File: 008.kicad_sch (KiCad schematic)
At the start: 38 parts, among them U1 AM6232ASCGHAALWR, U2 4Gbit

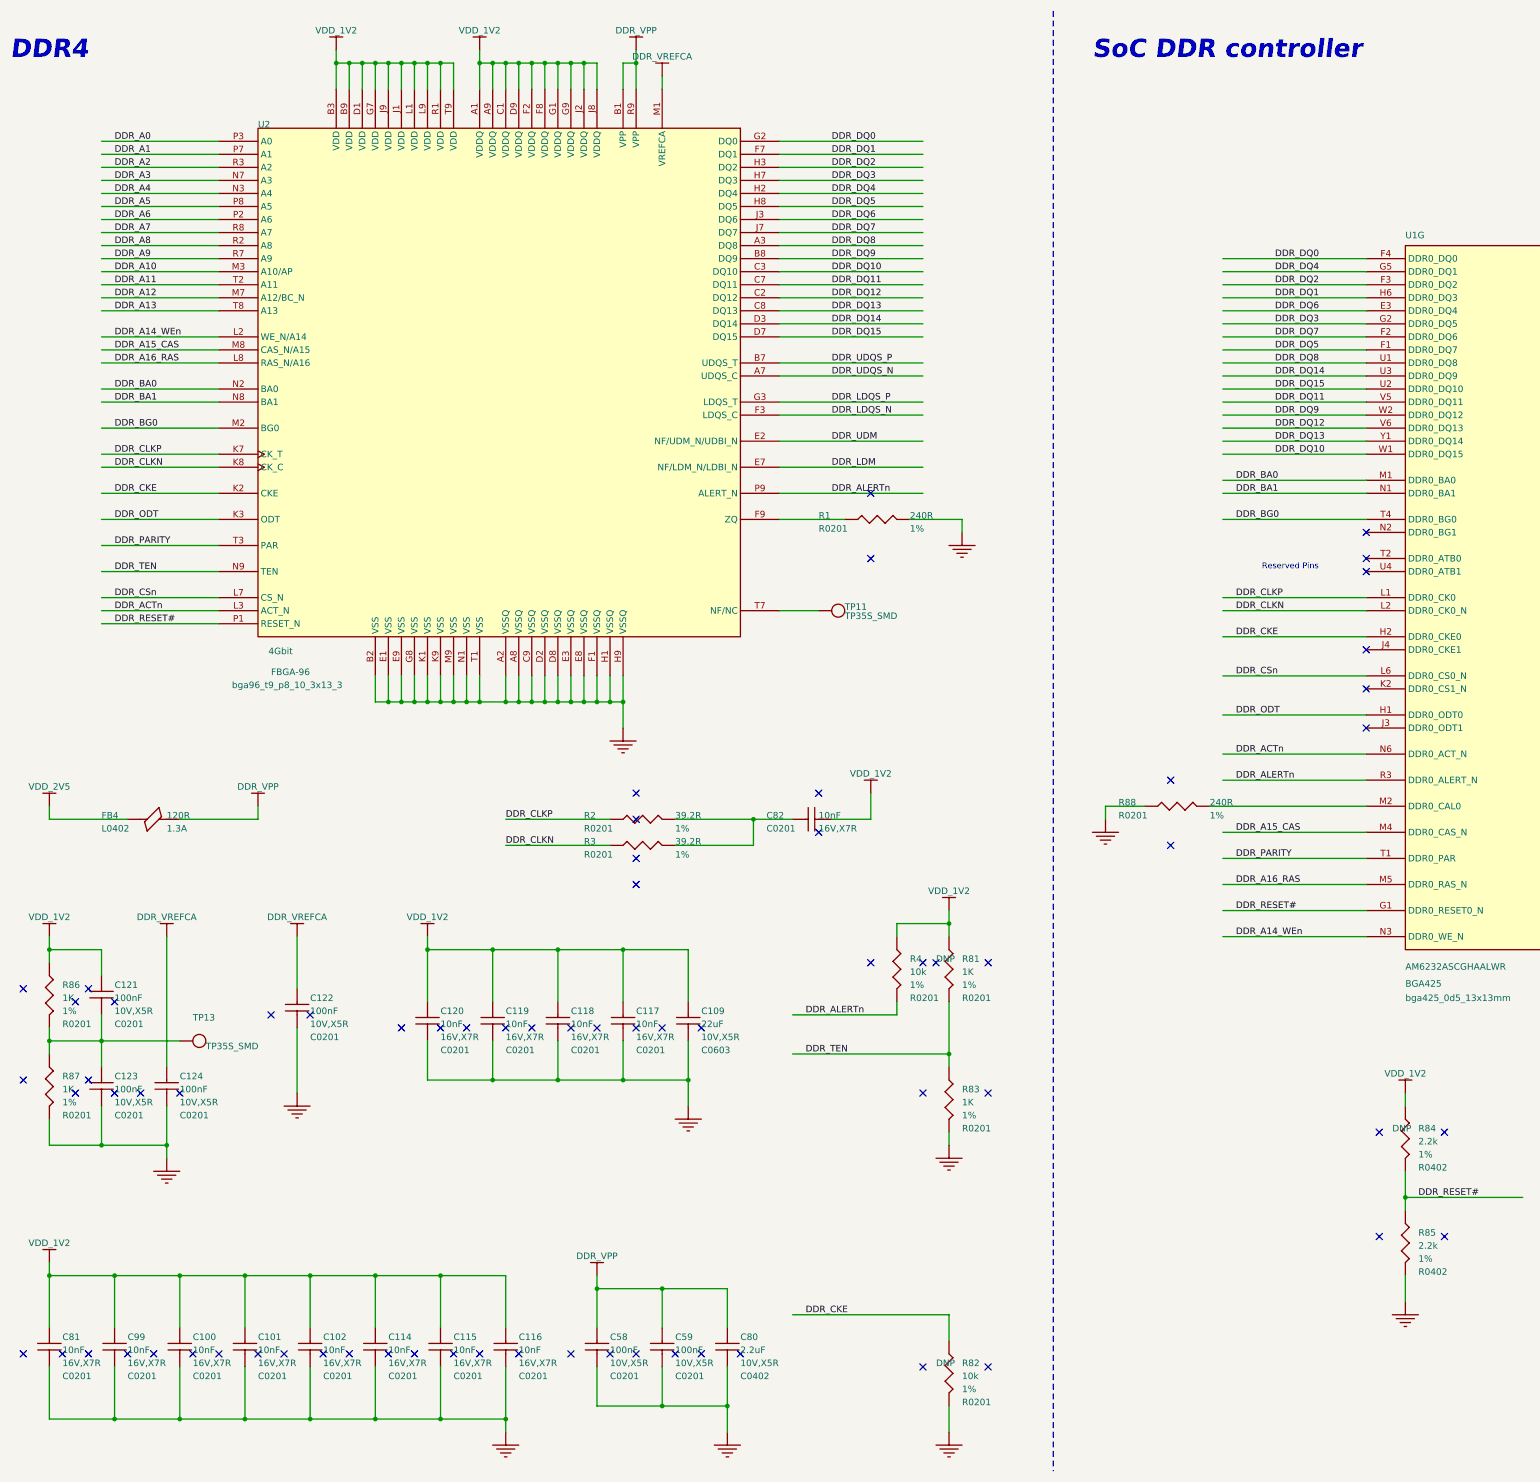
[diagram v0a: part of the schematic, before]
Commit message: Remove rando NCs added during conversion
Also a little tidying.

TODO: check junctions that may be missing. Noticed a few obvious ones
and corrected them already.

Signed-off-by: Michael Welling <mwelling79@gmail.com>
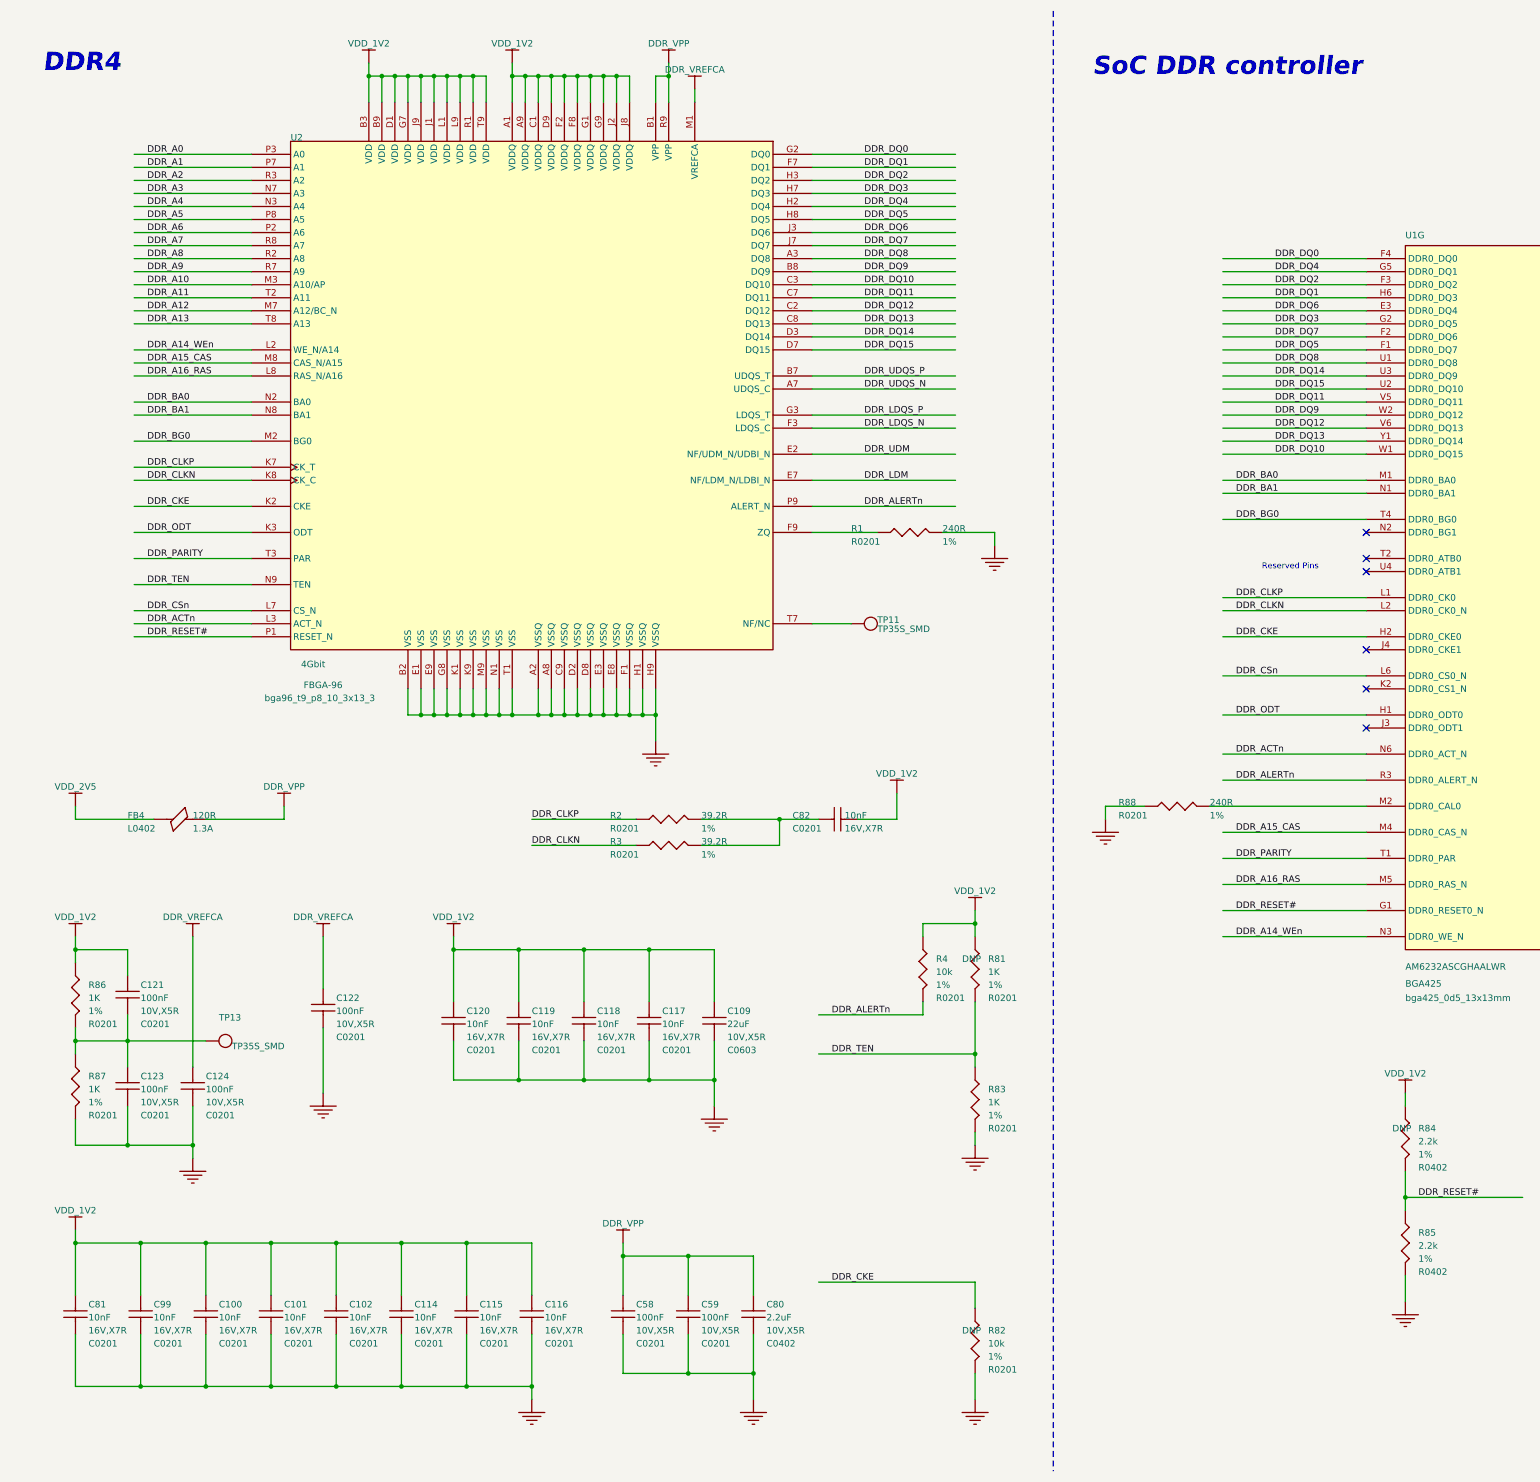
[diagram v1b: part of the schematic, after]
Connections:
- no-connect marks 72 -> 6
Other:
- moved on the sheet: C100, C101, C102, C109, C114, C115, C116, C117, C118, C119, C120, C121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

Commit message: Another round of cleansing fire
Signed-off-by: Michael Welling <mwelling79@gmail.com>
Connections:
- net DDR_VREFCA: now also C121.2, C123.1, R86.2, R87.1, TP13.1 (TP)
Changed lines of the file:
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@@
+	)
+	(junction
+		(at 43.18 208.28)
+		(diameter 0)
+		(color 0 0 0 0)
 	)
 	(junction
@@
 	(wire
 		(pts
+			(xy 43.18 208.28) (xy 43.18 187.96)
+		)
+		(stroke
+			(width 0)
+			(type default)
+		)
+	)
+	(wire
+		(pts
 			(xy 279.4 241.3) (xy 279.4 238.76)
 		)
@@
 	(wire
 		(pts
+			(xy 43.18 208.28) (xy 45.72 208.28)
+		)
+		(stroke
+			(width 0)
+			(type default)
+		)
+	)
+	(wire
+		(pts
 			(xy 406.4 86.36) (xy 378.46 86.36)
 		)
@@
 	(wire
 		(pts
-			(xy 30.48 208.28) (xy 45.72 208.28)
+			(xy 30.48 208.28) (xy 43.18 208.28)
 		)
 		(stroke
@@
 	(wire
 		(pts
-			(xy 43.18 213.36) (xy 43.18 187.96)
-		)
-		(stroke
+			(xy 43.18 213.36) (xy 43.18 208.28)
+		)
+		(stroke
